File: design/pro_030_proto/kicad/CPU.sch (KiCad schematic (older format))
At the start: 18 parts, among them IC1 MC68030RC_PGA, X1 33MHz

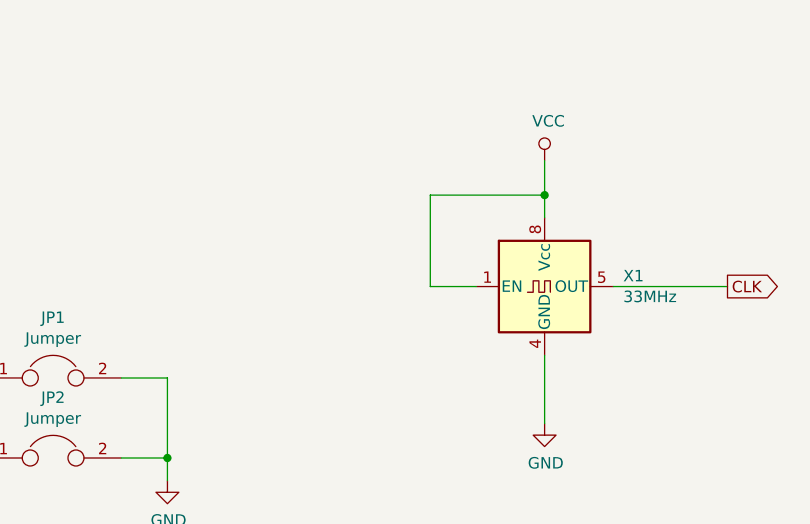
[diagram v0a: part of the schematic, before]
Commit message: Lots more changes
* Add DIN expansion connectors (provisional pinout)
* Fix incorrect address lines for RAM & ROM (Doh!)
* Remove unused level shifters
* Fix clock enables
* Lots of other small fixes
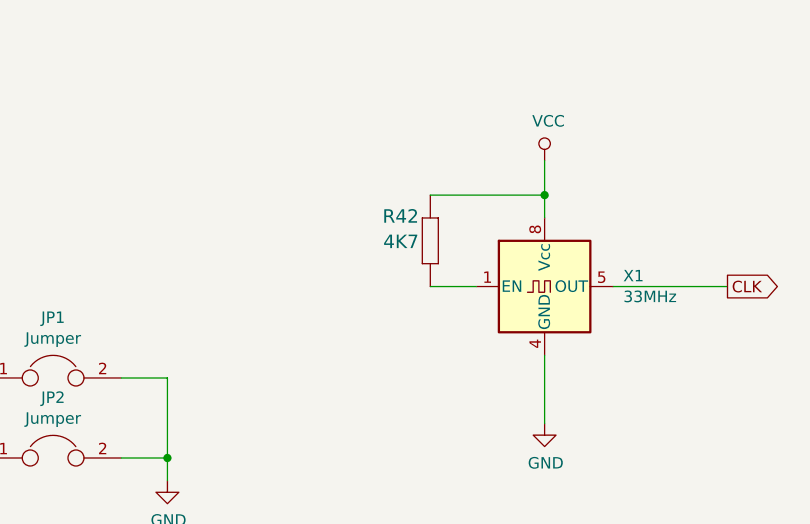
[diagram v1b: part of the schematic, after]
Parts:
- added R42: 4K7, rosco_m68k:R-0207_10, symbol rosco_m68k-eagle-import:R-EU_0207_10
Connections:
- net VCC: now also R42.2; no longer X1.1 (EN)
- new net: R42.1, X1.1 (EN)
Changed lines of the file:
@@
 $Descr A4 11693 8268
 encoding utf-8
-Sheet 2 15
+Sheet 2 14
 Title "rosco_m68k Pro (030) Prototype"
 Date "2021-10-01"
@@
 GND
 Wire Wire Line
-	7900 1650 7900 1250
-Wire Wire Line
 	7900 1250 8400 1250
 Connection ~ 8400 1250
 Wire Wire Line
 	8400 1250 8400 1350
+$Comp
+L rosco_m68k-eagle-import:R-EU_0207_10 R?
+U 1 1 619838B5
+P 7900 1450
+AR Path="/619838B5" Ref="R?"  Part="1"
+AR Path="/5E53B952/619838B5" Ref="R?"  Part="1"
+AR Path="/60FBFA5C/619838B5" Ref="R?"  Part="1"
+AR Path="/61043B8D/619838B5" Ref="R?"  Part="1"
+AR Path="/60EC67C5/619838B5" Ref="R42"  Part="1"
+F 0 "R42" V 8041 1500 59  0000 L BNN
+F 1 "4K7" V 7930 1500 59  0000 L BNN
+F 2 "rosco_m68k:R-0207_10" H 7900 1450 50  0001 C CNN
+F 3 "" H 7900 1450 50  0001 C CNN
+	1    7900 1450
+	0    -1   -1   0
+$EndComp
 $EndSCHEMATC
